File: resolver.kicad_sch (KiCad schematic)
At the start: 17 parts

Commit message: started adding AD2S
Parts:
- removed C20: 1uF, Capacitor_SMD:C_0603_1608Metric, symbol prius_gen2-rescue:C-Device-prius_gen2-rescue
- removed C21: 100uF, Capacitor_SMD:C_Elec_6.3x7.7, symbol prius_gen2-rescue:C-Device-prius_gen2-rescue
- removed C22, C23, C24, C25, C27: 22n, Capacitor_SMD:C_0603_1608Metric, symbol prius_gen2-rescue:C-Device-prius_gen2-rescue
- removed C26: 10u, Capacitor_SMD:C_0603_1608Metric, symbol prius_gen2-rescue:C-Device-prius_gen2-rescue
- removed C28, C29: 100n, Capacitor_SMD:C_0603_1608Metric, symbol prius_gen2-rescue:C-Device-prius_gen2-rescue
- removed R27: 330, Resistor_SMD:R_0603_1608Metric, symbol prius_gen2-rescue:R-Device-prius_gen2-rescue
- removed R28: 6.8k, Resistor_SMD:R_0603_1608Metric, symbol prius_gen2-rescue:R-Device-prius_gen2-rescue
- removed R29, R30: 10k, Resistor_SMD:R_0603_1608Metric, symbol prius_gen2-rescue:R-Device-prius_gen2-rescue
- removed R31, R32: 4.7, Resistor_SMD:R_0603_1608Metric, symbol prius_gen2-rescue:R-Device-prius_gen2-rescue
- removed U4: (no value), symbol prius_gen2-rescue:TDA2822D-TDA2822D-prius_gen2-rescue
- added C18, C19: 20pF, Capacitor_SMD:C_0603_1608Metric, symbol Device:C
- added R19, R20: 68k, symbol Device:R
- added U3: AD2S1205YSTZ, QFP80P1200X1200X160-44N, symbol AD2S1205YSTZ:AD2S1205YSTZ
- added Y2: 8.192MHz, Crystal:Crystal_SMD_5032-2Pin_5.0x3.2mm, symbol Device:Crystal
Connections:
- net +5V: now also U3.1 (DVDD_2), U3.17 (DVDD), U3.5 (RDVEL*)
- net GND: now also C18.1, C19.1, U3.16 (DGND_2), U3.23 (DGND), U3.3 (CS*), U3.6 (SOE*)
- new net: C18.2, U3.21 (XTALOUT), Y2.1
- new net CLKIN: C19.2, U3.22 (CLKIN), Y2.2
- new net COS: R19.1, U3.41 (COS)
- new net SCLK: U3.8 (DB10/SCLK)
- new net SIN: R20.1, U3.37 (SIN)
- new net SO: U3.7 (DB11/SO)
- new net ~{COS}: R19.2, U3.40 (COSLO)
- new net ~{RD}: U3.2 (RD*)
- new net ~{SAMPLE}: U3.4 (SAMPLE*)
- new net ~{SIN}: R20.2, U3.38 (SINLO)
- no-connect marks 0 -> 10
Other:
- note removed: "Resolver Excitation"

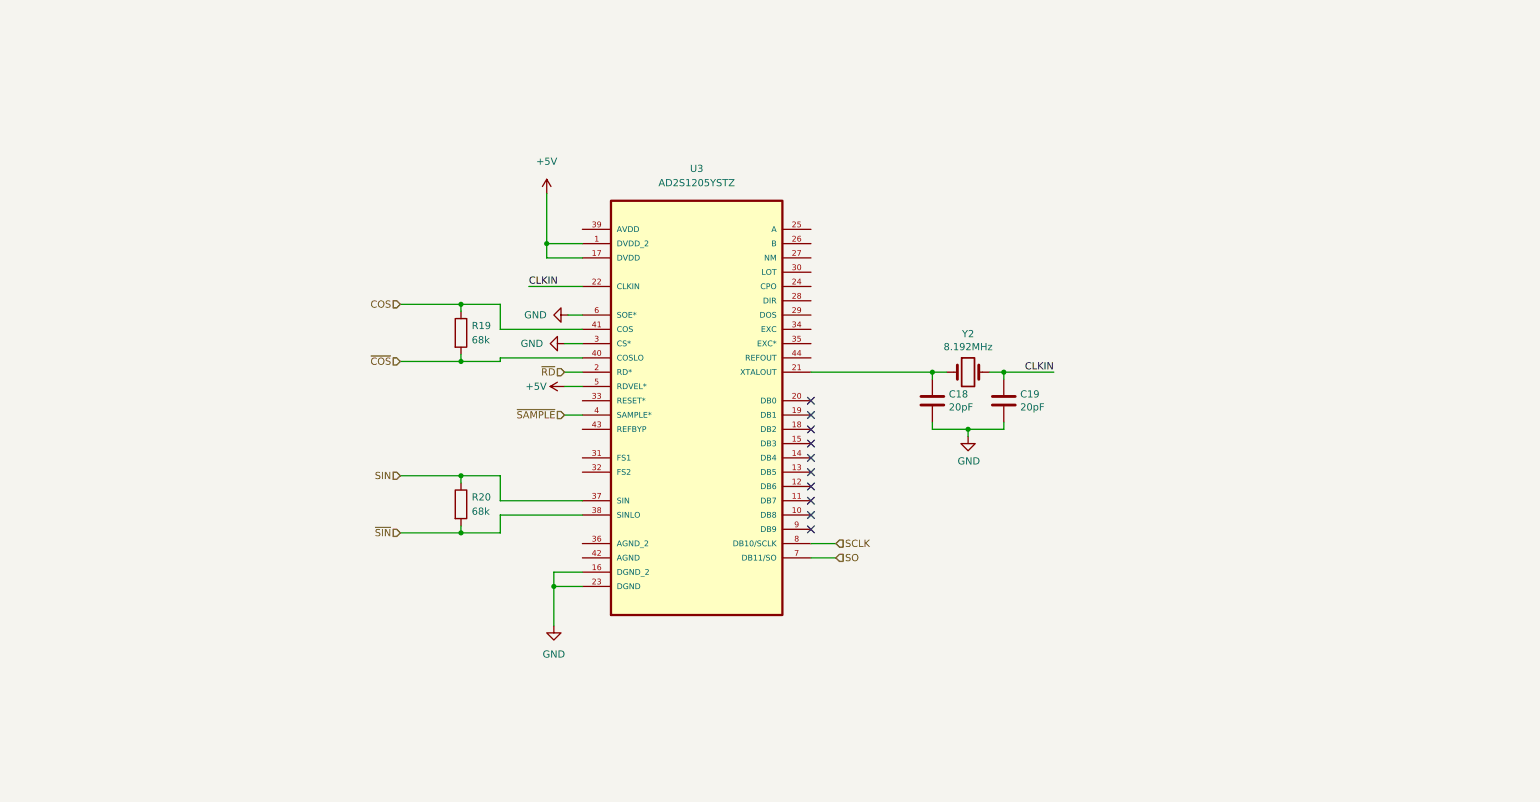
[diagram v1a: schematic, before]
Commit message: routed ad2s
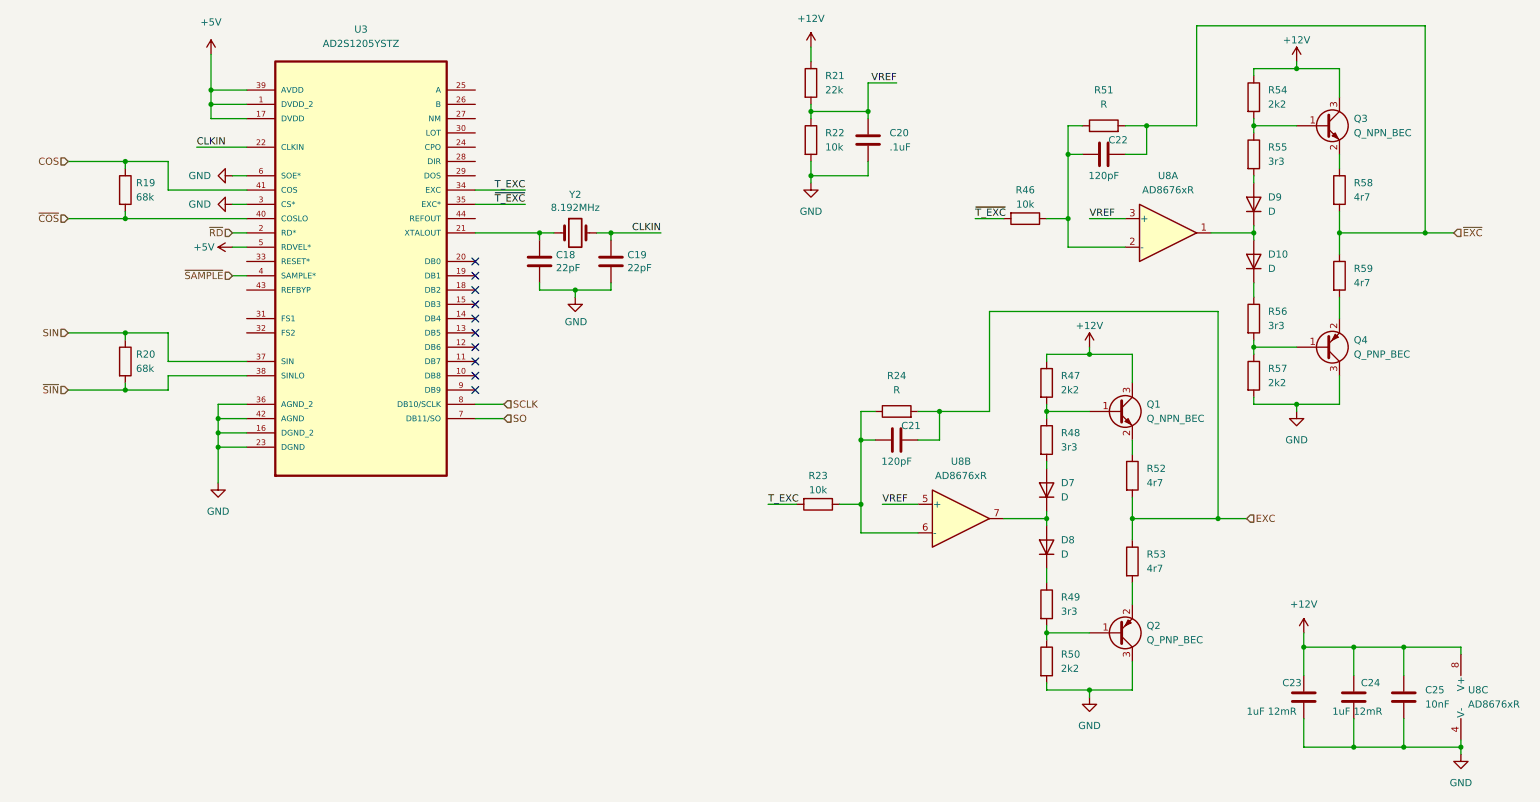
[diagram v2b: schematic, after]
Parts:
- added C20: .1uF, Capacitor_SMD:C_0603_1608Metric, symbol Device:C
- added C21, C22: 120pF, Capacitor_SMD:C_0603_1608Metric, symbol Device:C
- added C23, C24: 1uF 12mR, Capacitor_SMD:C_0603_1608Metric, symbol Device:C
- added C25: 10nF, Capacitor_SMD:C_0603_1608Metric, symbol Device:C
- added D10, D7, D8, D9: D, Diode_SMD:D_SOD-123, symbol Device:D
- added Q1, Q3: Q_NPN_BEC, Package_TO_SOT_SMD:TSOT-23, symbol Device:Q_NPN_BEC
- added Q2, Q4: Q_PNP_BEC, Package_TO_SOT_SMD:TSOT-23, symbol Device:Q_PNP_BEC
- added R21: 22k, Resistor_SMD:R_0603_1608Metric, symbol Device:R
- added R22, R23, R46: 10k, Resistor_SMD:R_0603_1608Metric, symbol Device:R
- added R24, R51: R, Resistor_SMD:R_0603_1608Metric, symbol Device:R
- added R47, R50, R54, R57: 2k2, Resistor_SMD:R_0603_1608Metric, symbol Device:R
- added R48, R49, R55, R56: 3r3, Resistor_SMD:R_0603_1608Metric, symbol Device:R
- added R52, R53, R58, R59: 4r7, Resistor_SMD:R_0603_1608Metric, symbol Device:R
- added U8: AD8676xR, Package_SO:SOIC-8_3.9x4.9mm_P1.27mm, symbol Amplifier_Operational:AD8676xR
- C18, C19: value 20pF -> 22pF; LCSC C105621 -> C309441
- R19, R20: footprint (none) -> Resistor_SMD:R_0603_1608Metric; LCSC (none) -> C23231
- U3: footprint QFP80P1200X1200X160-44N -> ad2s:QFP80P1200X1200X160-44N
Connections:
- net +5V: now also U3.39 (AVDD)
- net GND: now also U3.36 (AGND_2), U3.42 (AGND), C20.2, C23.2, C24.2, C25.2, Q2.3 (C), Q4.3 (C), R22.2, R50.2, R57.2, U8.4 (V-)
- net T_EXC: now reaches U3.34 (EXC)
- net T_EXC: now also R23.2
- net ~{T_EXC}: now reaches U3.35 (EXC*)
- net ~{T_EXC}: now also R46.2
- new net: Q1.1 (B), R47.2, R48.1
- new net: D7.2 (A), R48.2
- new net: C21.1, R23.1, R24.1, U8.6 (-)
- new net: Q3.2 (E), R58.1
- new net: Q3.1 (B), R54.2, R55.1
- new net: Q4.1 (B), R56.2, R57.1
- new net: Q2.1 (B), R49.2, R50.1
- new net: Q2.2 (E), R53.2
- new net: C22.1, R46.1, R51.1, U8.2 (-)
- new net: D10.1 (K), R56.1
- new net: D10.2 (A), D9.1 (K), U8.1
- new net: D8.1 (K), R49.1
- new net: Q1.2 (E), R52.1
- new net: D9.2 (A), R55.2
- new net: Q4.2 (E), R59.2
- new net: D7.1 (K), D8.2 (A), U8.7
- new net +12V: C23.1, C24.1, C25.1, Q1.3 (C), Q3.3 (C), R21.1, R47.1, R54.1, U8.8 (V+)
- new net EXC: C21.2, R24.2, R52.2, R53.1
- new net VREF: C20.1, R21.2, R22.1, U8.3 (+), U8.5 (+)
- new net ~{EXC}: C22.2, R51.2, R58.2, R59.1
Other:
- moved on the sheet: C18, C19, R19, R20, U3, Y2

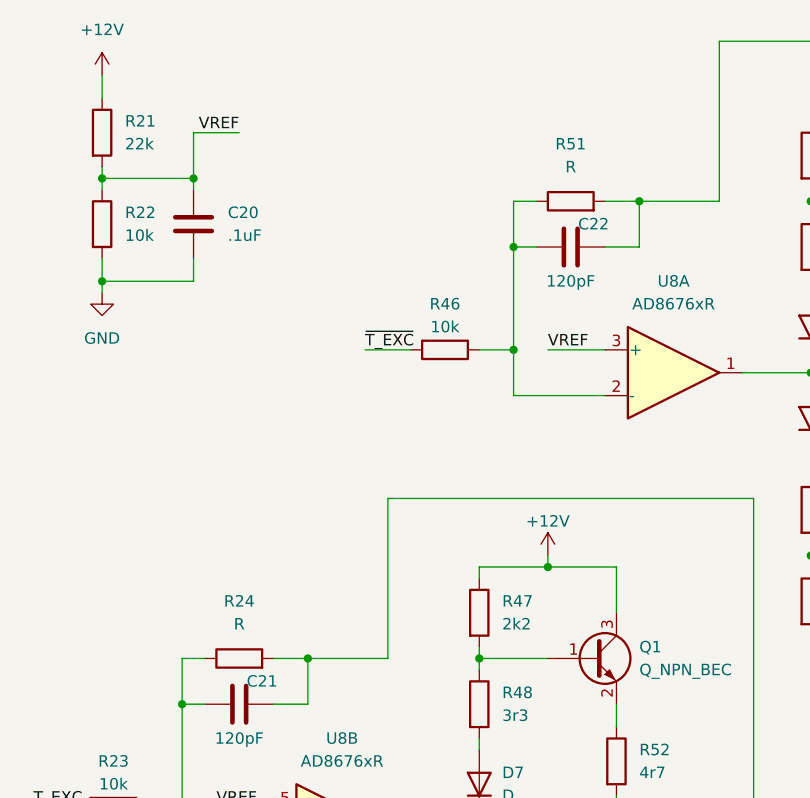
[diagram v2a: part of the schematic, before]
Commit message: fixed resolver buffer circuit
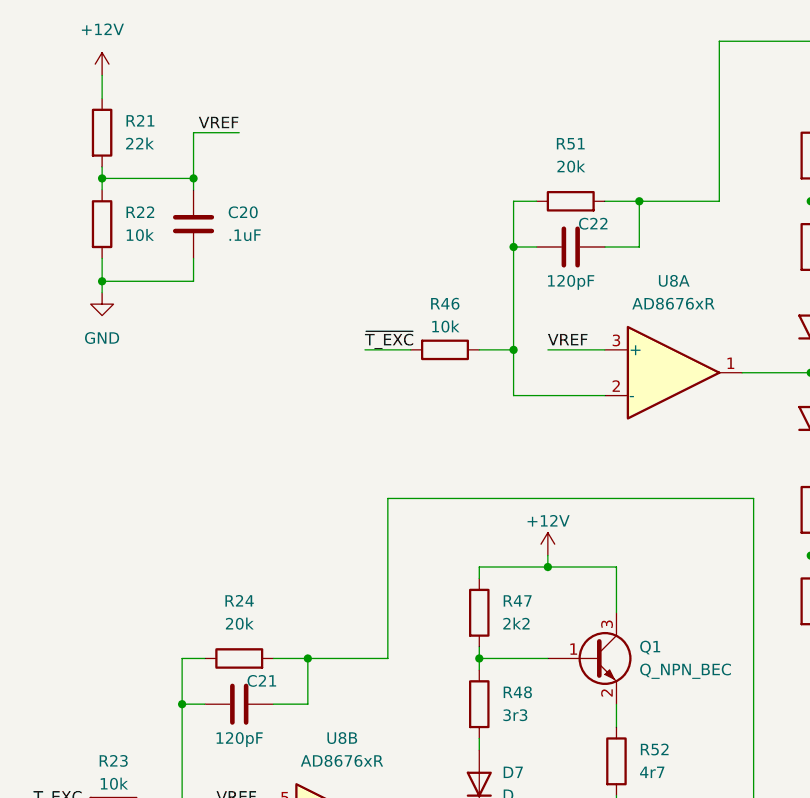
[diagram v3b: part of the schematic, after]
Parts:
- R24, R51: value R -> 20k
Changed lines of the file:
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@@
     (in_bom yes) (on_board yes) (fields_autoplaced)
     (property "Reference" "R51" (id 0) (at 209.55 33.02 90))
-    (property "Value" "R" (id 1) (at 209.55 35.56 90))
+    (property "Value" "20k" (id 1) (at 209.55 35.56 90))
     (property "Footprint" "Resistor_SMD:R_0603_1608Metric" (id 2) (at 209.55 41.148 90)
       (effects (font (size 1.27 1.27)) hide)
@@
     (in_bom yes) (on_board yes) (fields_autoplaced)
     (property "Reference" "R24" (id 0) (at 172.72 83.82 90))
-    (property "Value" "R" (id 1) (at 172.72 86.36 90))
+    (property "Value" "20k" (id 1) (at 172.72 86.36 90))
     (property "Footprint" "Resistor_SMD:R_0603_1608Metric" (id 2) (at 172.72 91.948 90)
       (effects (font (size 1.27 1.27)) hide)

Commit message: added USB
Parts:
- R24, R51: value 20k -> 17.4k; LCSC (none) -> C269466
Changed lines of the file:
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@@
     (in_bom yes) (on_board yes) (fields_autoplaced)
     (property "Reference" "R51" (id 0) (at 209.55 33.02 90))
-    (property "Value" "20k" (id 1) (at 209.55 35.56 90))
+    (property "Value" "17.4k" (id 1) (at 209.55 35.56 90))
     (property "Footprint" "Resistor_SMD:R_0603_1608Metric" (id 2) (at 209.55 41.148 90)
       (effects (font (size 1.27 1.27)) hide)
     )
     (property "Datasheet" "~" (id 3) (at 209.55 39.37 0)
+      (effects (font (size 1.27 1.27)) hide)
+    )
+    (property "LCSC" "C269466" (id 4) (at 209.55 39.37 90)
       (effects (font (size 1.27 1.27)) hide)
     )
@@
     (in_bom yes) (on_board yes) (fields_autoplaced)
     (property "Reference" "R24" (id 0) (at 172.72 83.82 90))
-    (property "Value" "20k" (id 1) (at 172.72 86.36 90))
+    (property "Value" "17.4k" (id 1) (at 172.72 86.36 90))
     (property "Footprint" "Resistor_SMD:R_0603_1608Metric" (id 2) (at 172.72 91.948 90)
       (effects (font (size 1.27 1.27)) hide)
@@
       (effects (font (size 1.27 1.27)) hide)
     )
+    (property "LCSC" "C269466" (id 4) (at 172.72 90.17 90)
+      (effects (font (size 1.27 1.27)) hide)
+    )

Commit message: v0.5 production files
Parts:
- U8: LCSC (none) -> C28133
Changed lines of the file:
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@@
+      (effects (font (size 1.27 1.27)) hide)
+    )
+    (property "LCSC" "C28133" (at 273.05 140.97 0)
       (effects (font (size 1.27 1.27)) hide)
     )
@@
       (effects (font (size 1.27 1.27)) hide)
     )
+    (property "LCSC" "C28133" (at 220.98 58.42 0)
+      (effects (font (size 1.27 1.27)) hide)
+    )
     (pin "1")
     (pin "2")
@@
       (effects (font (size 1.27 1.27)) hide)
     )
+    (property "LCSC" "C28133" (at 184.15 109.22 0)
+      (effects (font (size 1.27 1.27)) hide)
+    )
